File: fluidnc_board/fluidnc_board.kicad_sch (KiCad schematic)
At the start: 0 parts

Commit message: esp32 and motor driver stuff
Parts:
- added J?: Micro_SD_Card, symbol Connector:Micro_SD_Card
- added R? (x2): 4.7k, symbol Device:R
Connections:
- new net +3V3: J?.4 (VDD), R?.1, R?.1
- new net GND: J?.6 (VSS), J?.9 (SHIELD)
- new net MISO: J?.7 (DAT0)
- new net MOSI: J?.3 (CMD)
- new net SCK: J?.5 (CLK)
- new net SCL: R?.2
- new net SDA: R?.2
- new net SD_CS: J?.2 (DAT3/CD)
- no-connect marks 0 -> 2
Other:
- added sheet esp32 (esp32.kicad_sch)
- added sheet i2so (i2so.kicad_sch)
- added sheet power_supply (power_supply.kicad_sch)
- added sheet switches (switches.kicad_sch)
- sheet motor_drivers ports: added CS_E, CS_X, CS_Y, CS_Z, DIR_E, DIR_X, DIR_Y, DIR_Z, EN_E, EN_X, EN_Y, EN_Z, MISO, MOSI, SCK, STEP_E, STEP_X, STEP_Y, STEP_Z; removed none

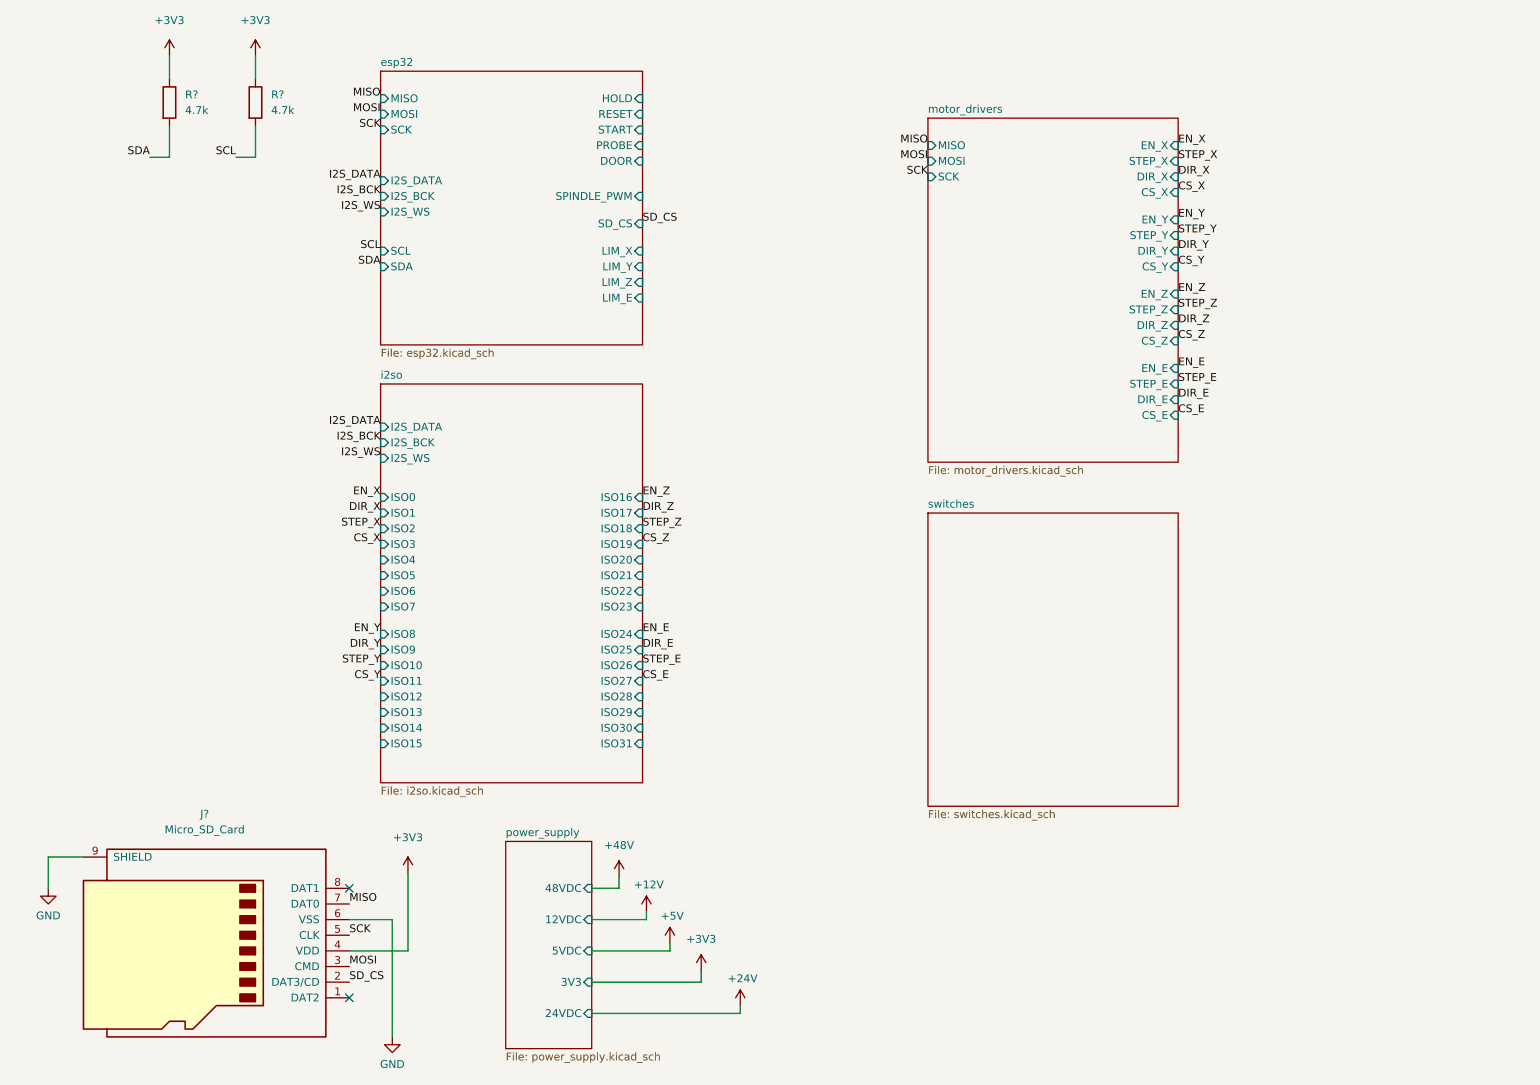
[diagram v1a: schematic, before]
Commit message: outputs, spindle output and switch inputs
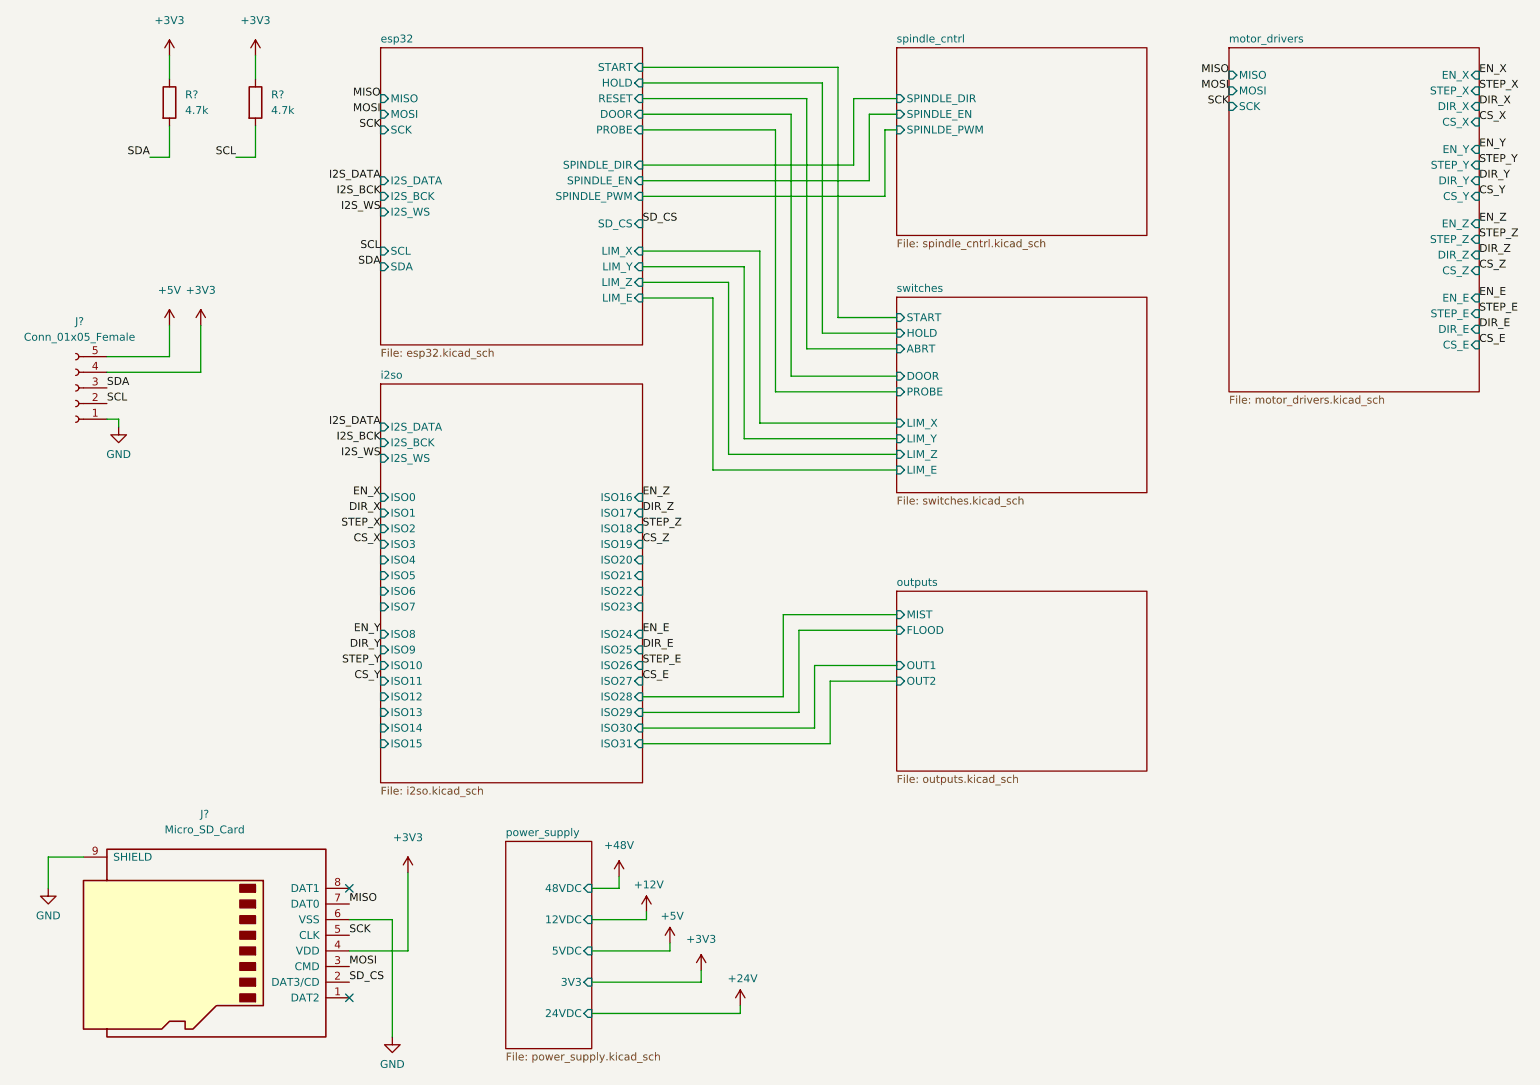
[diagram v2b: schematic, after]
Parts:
- added J?: Conn_01x05_Female, symbol Connector:Conn_01x05_Female
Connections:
- net +3V3: now also J?.4 (Pin_4)
- net +5V: now also J?.5 (Pin_5)
- net GND: now also J?.1 (Pin_1)
- net SCL: now also J?.2 (Pin_2)
- net SDA: now also J?.3 (Pin_3)
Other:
- added sheet outputs (outputs.kicad_sch)
- added sheet spindle_cntrl (spindle_cntrl.kicad_sch)
- sheet esp32 ports: added SPINDLE_DIR, SPINDLE_EN; removed none
- sheet switches ports: added ABRT, DOOR, HOLD, LIM_E, LIM_X, LIM_Y, LIM_Z, PROBE, START; removed none

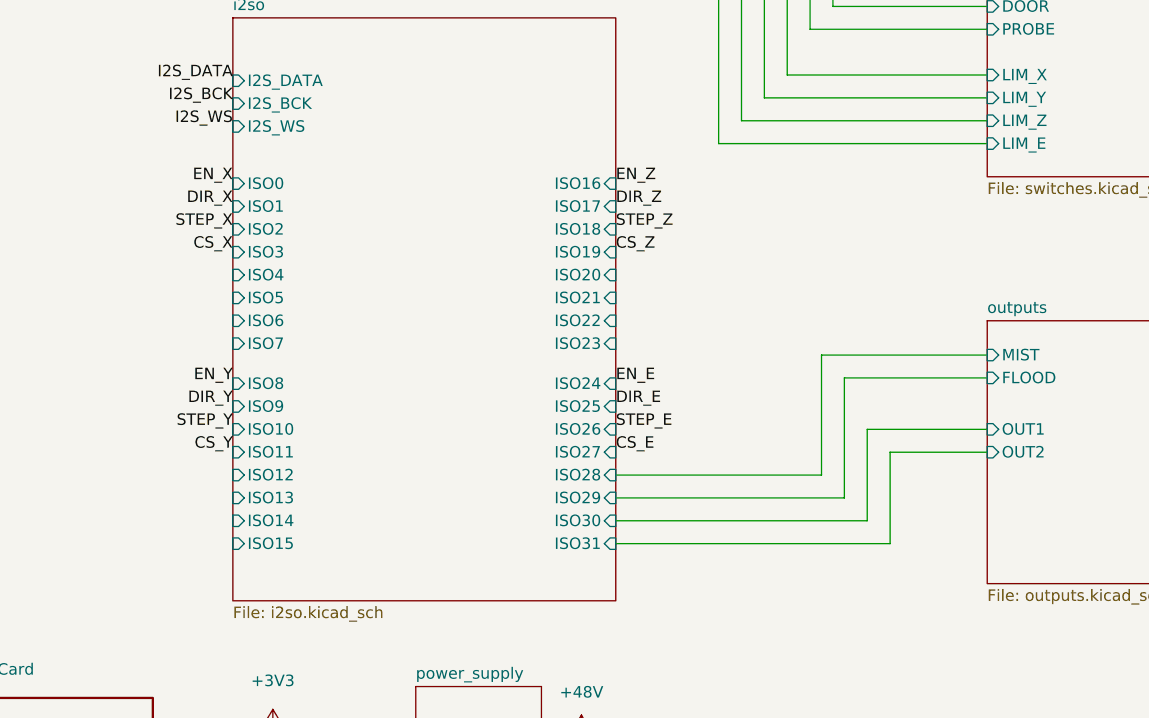
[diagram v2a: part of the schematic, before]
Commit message: remove unnecessary i2s chip
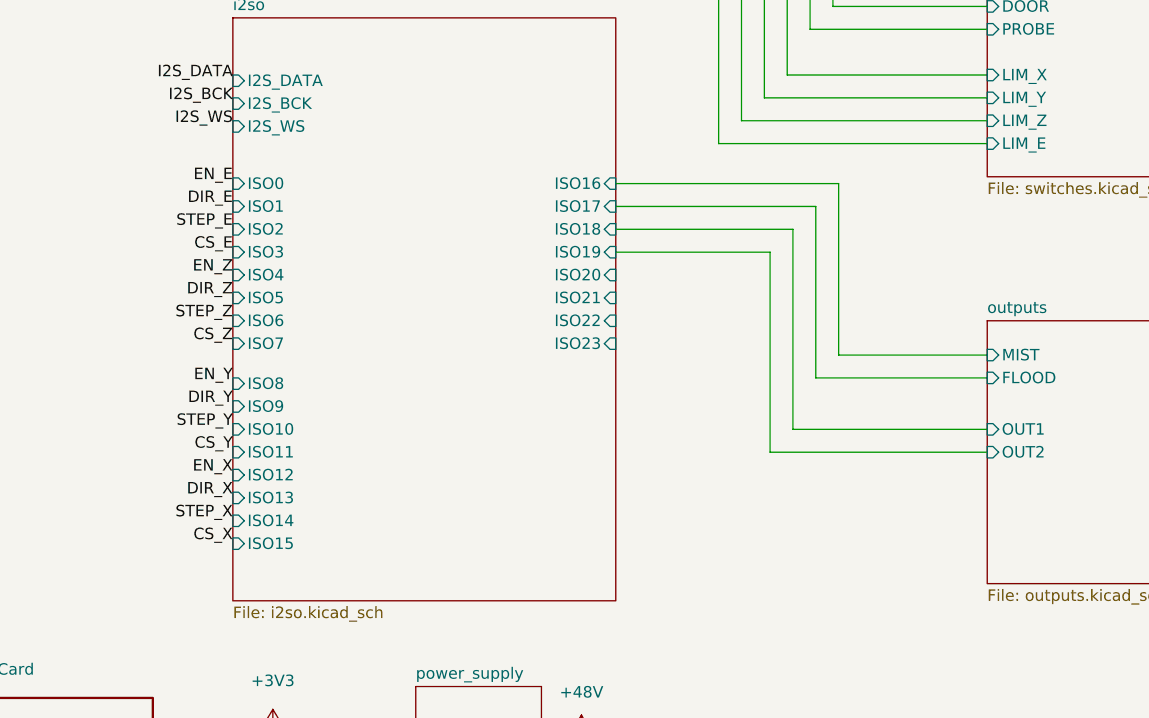
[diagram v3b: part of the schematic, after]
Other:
- sheet i2so ports: added none; removed ISO24, ISO25, ISO26, ISO27, ISO28, ISO29, ISO30, ISO31
- title: (none) -> FluidNC Board

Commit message: footprint associations and part no.
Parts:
- removed J?: Micro_SD_Card, symbol Connector:Micro_SD_Card
- added J2: Micro_SD_Card_Det, Connector_Card:microSD_HC_Molex_104031-0811, symbol Connector:Micro_SD_Card_Det
- J1: renamed from J?; footprint (none) -> Connector_JST:JST_XH_B5B-XH-AM_1x05_P2.50mm_Vertical
- R1, R2: renamed from R?; value 4.7k -> 3k; footprint (none) -> Resistor_SMD:R_0603_1608Metric_Pad0.98x0.95mm_HandSolder; Digikey Part No. (none) -> 311-3.00KHRCT-ND
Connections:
- net +3V3: now also J2.4 (VDD)
- net GND: now also J2.11 (SHIELD), J2.6 (VSS)
- net MISO: now also J2.7 (DAT0)
- net MOSI: now also J2.3 (CMD)
- net SCK: now also J2.5 (CLK)
- net SD_CS: now also J2.2 (DAT3/CD)
- no-connect marks 2 -> 4

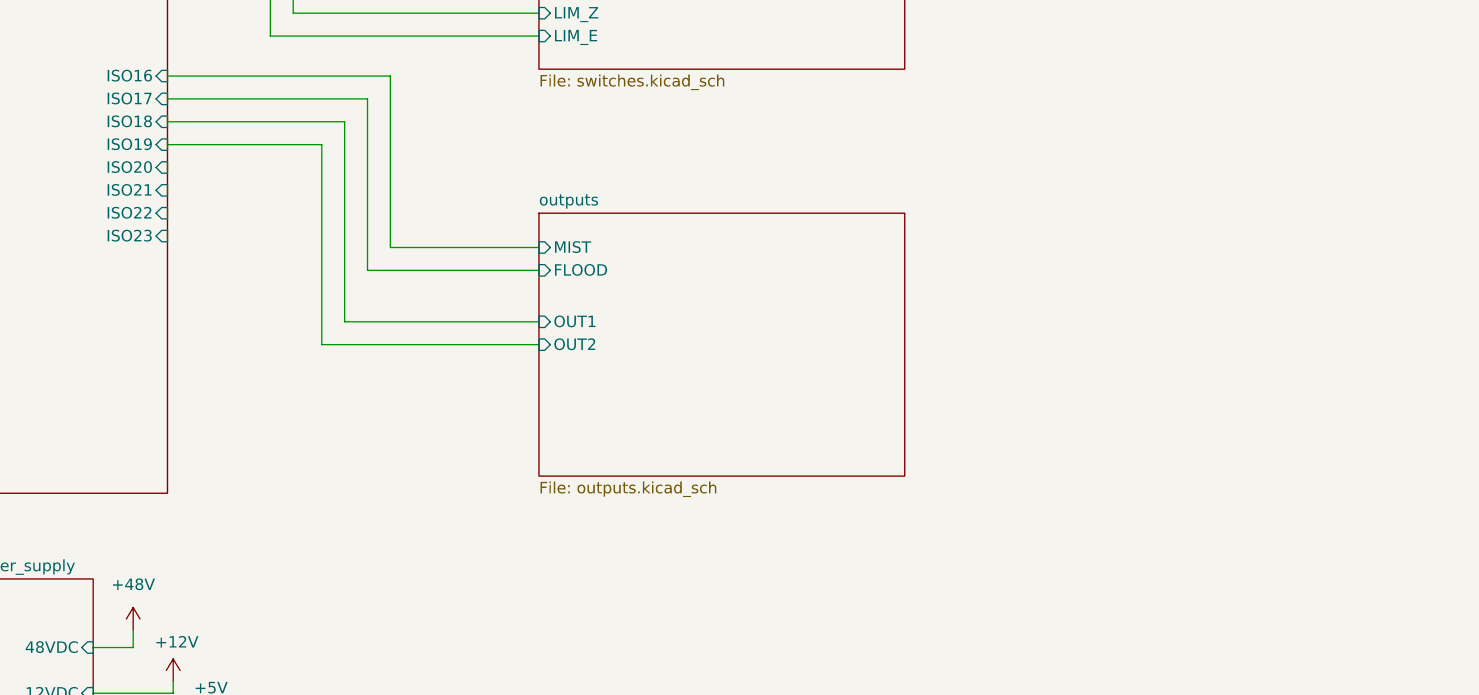
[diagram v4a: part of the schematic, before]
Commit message: fix some footprint associations
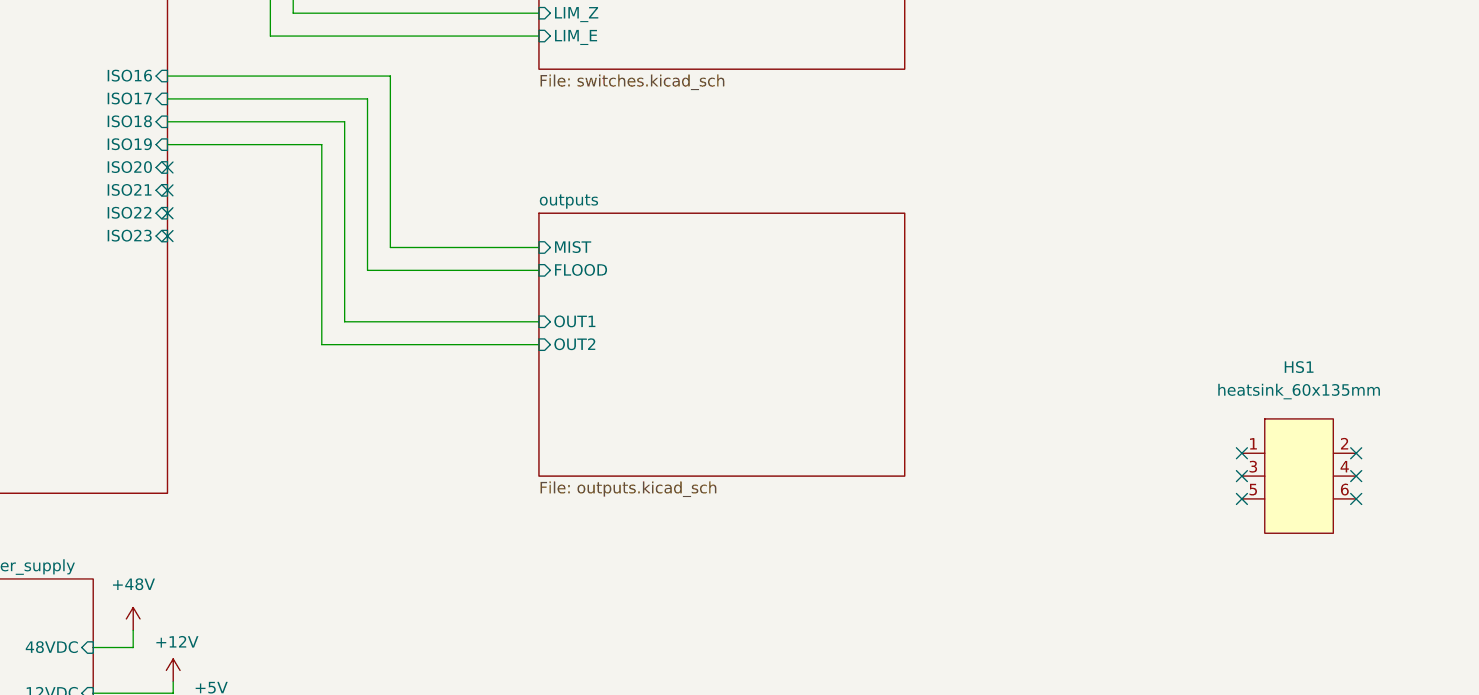
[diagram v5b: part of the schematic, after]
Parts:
- added HS1: heatsink_60x135mm, fluidnc_board:heatsink_60x135mm, symbol fluidnc_board:heatsink_60x135mm
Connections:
- no-connect marks 4 -> 14
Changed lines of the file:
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@@
   (no_connect (at 76.2 160.655))
   (no_connect (at 76.2 158.115))
+  (no_connect (at 123.825 117.475))
+  (no_connect (at 123.825 114.935))
+  (no_connect (at 123.825 112.395))
+  (no_connect (at 123.825 109.855))
+  (no_connect (at 255.905 141.605))
+  (no_connect (at 255.905 144.145))
+  (no_connect (at 255.905 146.685))
+  (no_connect (at 243.205 146.685))
+  (no_connect (at 243.205 144.145))
+  (no_connect (at 243.205 141.605))
   (no_connect (at 76.2 163.195))
   (no_connect (at 76.2 180.975))
@@
   (label "CS_Z" (at 81.28 117.475 180)
     (effects (font (size 1.27 1.27)) (justify right bottom))
+  )
+  (symbol (lib_id "fluidnc_board:heatsink_60x135mm") (at 249.555 144.145 0) (unit 1)
+    (in_bom yes) (on_board yes) (fields_autoplaced)
+    (property "Reference" "HS1" (id 0) (at 249.555 132.08 0))
+    (property "Value" "heatsink_60x135mm" (id 1) (at 249.555 134.62 0))
+    (property "Footprint" "fluidnc_board:heatsink_60x135mm" (id 2) (at 249.555 133.985 0)
+      (effects (font (size 1.27 1.27)) hide)
+    )
+    (property "Datasheet" "" (id 3) (at 257.175 149.225 0)
+      (effects (font (size 1.27 1.27)) hide)
+    )
+    (pin "1")
+    (pin "2")
+    (pin "3")
+    (pin "4")
+    (pin "5")
+    (pin "6")
   )
   (symbol (lib_id "power:+24V") (at 139.7 182.245 0) (unit 1)
@@
       (reference "F3") (unit 1) (value "2A") (footprint "Fuse:Fuse_Bourns_MF-RHT200")
     )
+    (path "/09df09f9-7e69-4f19-b986-6fba4d8264e5"
+      (reference "HS1") (unit 1) (value "heatsink_60x135mm") (footprint "fluidnc_board:heatsink_60x135mm")
+    )
     (path "/6adebb0a-cdb4-442d-87a4-d4149b99f646"
       (reference "J1") (unit 1) (value "Conn_01x05_Female") (footprint "Connector_JST:JST_XH_B5B-XH-AM_1x05_P2.50mm_Vertical")
@@
     )
     (path "/411ae353-442c-45cb-a1bd-bf9deb010d80/f6a7fe1a-11f1-4160-8f8c-04a3ec4da628/dd64de23-f859-428f-a732-e18e01786856"
-      (reference "U5") (unit 1) (value "TMC5160_SILENTSTEPSTICK") (footprint "grbl_board:TMC5160_SILENTSTEPSTICK")
+      (reference "U5") (unit 1) (value "TMC5160_SILENTSTEPSTICK") (footprint "fluidnc_board:TMC5160_SILENTSTEPSTICK")
     )
     (path "/411ae353-442c-45cb-a1bd-bf9deb010d80/58eabbec-ba95-479f-b316-5dcc9482b7d1/06f64e66-0653-4e18-85a3-5a05f4b03ae8"
@@
     )
     (path "/411ae353-442c-45cb-a1bd-bf9deb010d80/58eabbec-ba95-479f-b316-5dcc9482b7d1/dd64de23-f859-428f-a732-e18e01786856"
-      (reference "U9") (unit 1) (value "TMC5160_SILENTSTEPSTICK") (footprint "grbl_board:TMC5160_SILENTSTEPSTICK")
+      (reference "U9") (unit 1) (value "TMC5160_SILENTSTEPSTICK") (footprint "fluidnc_board:TMC5160_SILENTSTEPSTICK")
     )
     (path "/411ae353-442c-45cb-a1bd-bf9deb010d80/04a6c528-c82a-4c2d-b1e2-922adffc267c/06f64e66-0653-4e18-85a3-5a05f4b03ae8"
@@
     )
     (path "/411ae353-442c-45cb-a1bd-bf9deb010d80/04a6c528-c82a-4c2d-b1e2-922adffc267c/dd64de23-f859-428f-a732-e18e01786856"
-      (reference "U13") (unit 1) (value "TMC5160_SILENTSTEPSTICK") (footprint "grbl_board:TMC5160_SILENTSTEPSTICK")
+      (reference "U13") (unit 1) (value "TMC5160_SILENTSTEPSTICK") (footprint "fluidnc_board:TMC5160_SILENTSTEPSTICK")
     )
     (path "/411ae353-442c-45cb-a1bd-bf9deb010d80/85e84d9c-d33a-42fe-961e-9d38ee8ee0f9/06f64e66-0653-4e18-85a3-5a05f4b03ae8"
@@
     )
     (path "/411ae353-442c-45cb-a1bd-bf9deb010d80/85e84d9c-d33a-42fe-961e-9d38ee8ee0f9/dd64de23-f859-428f-a732-e18e01786856"
-      (reference "U17") (unit 1) (value "TMC5160_SILENTSTEPSTICK") (footprint "grbl_board:TMC5160_SILENTSTEPSTICK")
+      (reference "U17") (unit 1) (value "TMC5160_SILENTSTEPSTICK") (footprint "fluidnc_board:TMC5160_SILENTSTEPSTICK")
     )
     (path "/ef38a5ba-2d3d-4f0a-bcbd-62e2cfbf5d52/fc9b3a92-91d8-4dc6-896d-26023ff41752"

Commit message: fixed some footprint associations, placed footprints
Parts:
- J2: Digikey Part No. WM6357CT-ND -> (none)
- R1, R2: Digikey Part No. 311-3.00KHRCT-ND -> (none)
